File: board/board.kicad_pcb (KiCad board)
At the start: 2 copper layers, 21 x 13 mm, 1 part

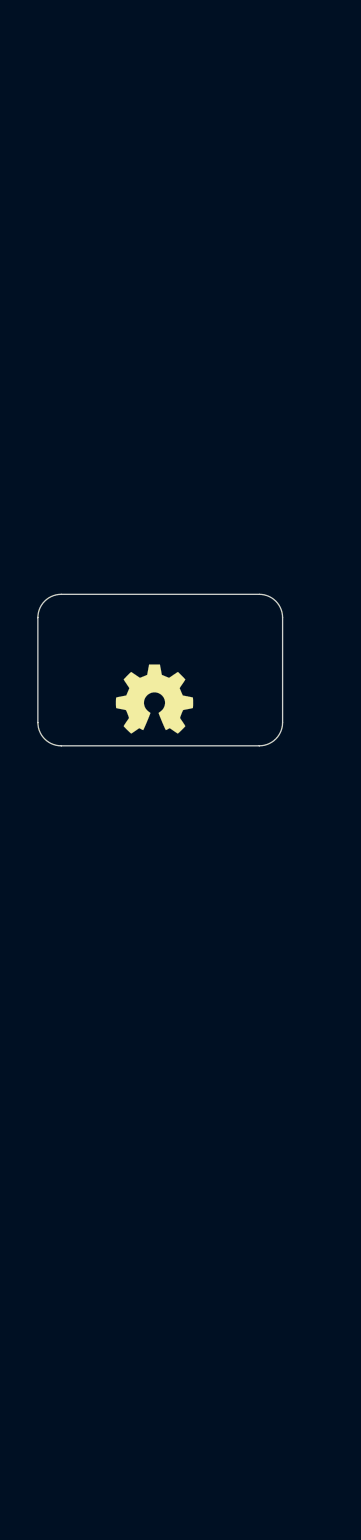
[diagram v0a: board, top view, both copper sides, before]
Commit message: added decoupling components
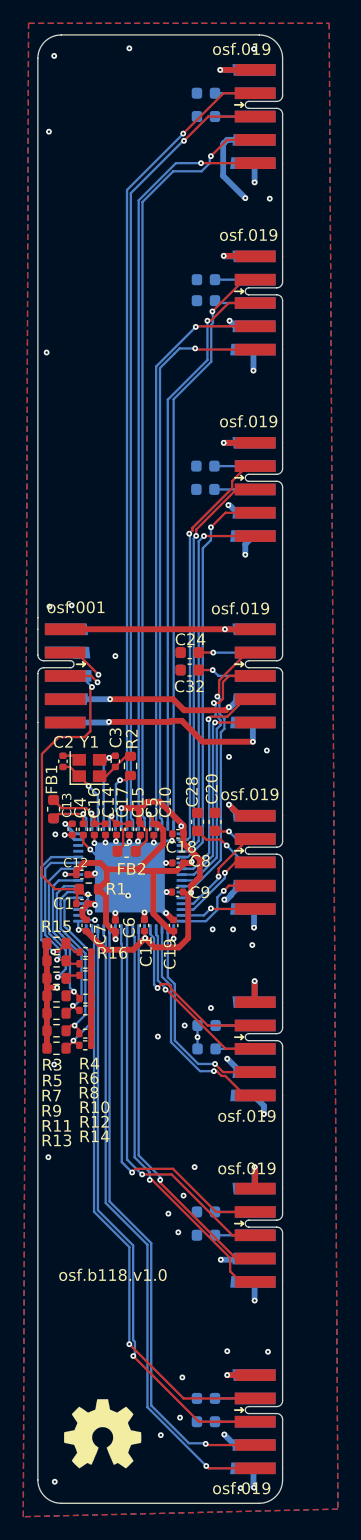
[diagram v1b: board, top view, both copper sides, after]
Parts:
- added C1: 10uF, Capacitor_SMD:C_0402_1005Metric, F.Cu at (143.8, 116.5)
- added C10: 1uF, Capacitor_SMD:C_0402_1005Metric, F.Cu at (149.9, 110.2)
- added C11: 1uF, Capacitor_SMD:C_0402_1005Metric, F.Cu at (149.2, 118.4)
- added C12: 1uF, Capacitor_SMD:C_0402_1005Metric, F.Cu at (143.8, 114.0)
- added C13: 1uF, Capacitor_SMD:C_0402_1005Metric, F.Cu at (142.9, 110.2)
- added C14: 10uF, Capacitor_SMD:C_0402_1005Metric, F.Cu at (145.8, 110.2)
- added C15: 10uF, Capacitor_SMD:C_0402_1005Metric, F.Cu at (147.8, 110.2)
- added C16: 1uF, Capacitor_SMD:C_0402_1005Metric, F.Cu at (144.8, 110.2)
- added C17: 1uF, Capacitor_SMD:C_0402_1005Metric, F.Cu at (146.8, 110.2)
- added C18: 1uF, Capacitor_SMD:C_0402_1005Metric, F.Cu at (152.0, 110.5)
- added C19: 1uF, Capacitor_SMD:C_0402_1005Metric, F.Cu at (151.7, 118.4)
- added C2: 22pF, Capacitor_SMD:C_0402_1005Metric, F.Cu at (142.2, 104.3)
- added C20: 100nF, Capacitor_SMD:C_0603_1608Metric, F.Cu at (155.2, 109.5)
- added C21: 100nF, Capacitor_SMD:C_0603_1608Metric, B.Cu at (154.5, 127.0)
- added C22: 100nF, Capacitor_SMD:C_0603_1608Metric, B.Cu at (154.4, 143.0)
- added C23: 100nF, Capacitor_SMD:C_0603_1608Metric, B.Cu at (154.4, 79.0)
- added C24: 100nF, Capacitor_SMD:C_0603_1608Metric, F.Cu at (153.0, 95.0)
- added C25: 100nF, Capacitor_SMD:C_0603_1608Metric, B.Cu at (154.4, 159.0)
- added C26: 100nF, Capacitor_SMD:C_0603_1608Metric, B.Cu at (154.4, 63.0)
- added C27: 100nF, Capacitor_SMD:C_0603_1608Metric, B.Cu at (154.4, 47.0)
- added C28: 100nF, Capacitor_SMD:C_0603_1608Metric, F.Cu at (153.7, 109.5)
- added C29: 100nF, Capacitor_SMD:C_0603_1608Metric, B.Cu at (154.5, 129.0)
- added C3: 22pF, Capacitor_SMD:C_0402_1005Metric, F.Cu at (146.7, 104.3)
- added C30: 100nF, Capacitor_SMD:C_0603_1608Metric, B.Cu at (154.4, 145.0)
- added C31: 100nF, Capacitor_SMD:C_0603_1608Metric, B.Cu at (154.4, 81.0)
- added C32: 100nF, Capacitor_SMD:C_0603_1608Metric, F.Cu at (153.0, 96.5)
- added C33: 100nF, Capacitor_SMD:C_0603_1608Metric, B.Cu at (154.4, 161.0)
- added C34: 100nF, Capacitor_SMD:C_0603_1608Metric, B.Cu at (154.4, 64.8)
- added C35: 100nF, Capacitor_SMD:C_0603_1608Metric, B.Cu at (154.4, 49.0)
- added C4: 10uF, Capacitor_SMD:C_0402_1005Metric, F.Cu at (143.9, 110.2)
- added C5: 10uF, Capacitor_SMD:C_0402_1005Metric, F.Cu at (148.8, 110.2)
- added C6: 1uF, Capacitor_SMD:C_0402_1005Metric, F.Cu at (146.7, 118.5)
- added C7: 1uF, Capacitor_SMD:C_0402_1005Metric, F.Cu at (144.2, 118.4)
- added C8: 1uF, Capacitor_SMD:C_0402_1005Metric, F.Cu at (152.0, 113.0)
- added C9: 1uF, Capacitor_SMD:C_0402_1005Metric, F.Cu at (152.0, 115.5)
- added FB1: Ferrite_Bead_Small, Inductor_SMD:L_0603_1608Metric, F.Cu at (141.3, 108.4)
- added FB2: Ferrite_Bead_Small, Inductor_SMD:L_0603_1608Metric, F.Cu at (147.6, 112.0)
- added IC1: RTL8305NB-CG, Package_DFN_QFN:QFN-64-1EP_9x9mm_P0.5mm_EP6x6mm, B.Cu at (147.9, 114.3)
- added J1: 001_I2C, on_edge:on_edge_2x05_device, F.Cu at (140.0, 97.0)
- added J2: 019_100BASE-T_with_CT, on_edge:on_edge_2x05_host, F.Cu at (161.0, 113.0)
- added J3: 019_100BASE-T_with_CT, on_edge:on_edge_2x05_host, F.Cu at (161.0, 129.0)
- added J4: 019_100BASE-T_with_CT, on_edge:on_edge_2x05_host, F.Cu at (161.0, 145.0)
- added J5: 019_100BASE-T_with_CT, on_edge:on_edge_2x05_host, F.Cu at (161.0, 161.0)
- added J6: 019_100BASE-T_with_CT, on_edge:on_edge_2x05_host, F.Cu at (161.0, 97.0)
- added J7: 019_100BASE-T_with_CT, on_edge:on_edge_2x05_host, F.Cu at (161.0, 65.0)
- added J8: 019_100BASE-T_with_CT, on_edge:on_edge_2x05_host, F.Cu at (161.0, 81.0)
- added J9: 019_100BASE-T_with_CT, on_edge:on_edge_2x05_host, F.Cu at (161.0, 49.0)
- added R1: 10k, Resistor_SMD:R_0603_1608Metric, F.Cu at (144.4, 115.3)
- added R10: d.n.p, Resistor_SMD:R_0402_1005Metric, F.Cu at (144.1, 125.7)
- added R11: 1k, Resistor_SMD:R_0603_1608Metric, F.Cu at (141.6, 127.5)
- added R12: d.n.p, Resistor_SMD:R_0402_1005Metric, F.Cu at (144.1, 127.7)
- added R13: 1k, Resistor_SMD:R_0603_1608Metric, F.Cu at (141.6, 128.9)
- added R14: d.n.p, Resistor_SMD:R_0402_1005Metric, F.Cu at (144.1, 128.7)
- added R15: 1k, Resistor_SMD:R_0603_1608Metric, F.Cu at (141.6, 120.0)
- added R16: d.n.p, Resistor_SMD:R_0402_1005Metric, F.Cu at (144.1, 120.7)
- added R2: 2.49k, Resistor_SMD:R_0603_1608Metric, F.Cu at (147.9, 104.7)
- added R3: 1k, Resistor_SMD:R_0603_1608Metric, F.Cu at (141.6, 121.5)
- added R4: d.n.p, Resistor_SMD:R_0402_1005Metric, F.Cu at (144.1, 121.7)
- added R5: 1k, Resistor_SMD:R_0603_1608Metric, F.Cu at (141.6, 123.0)
- added R6: d.n.p, Resistor_SMD:R_0402_1005Metric, F.Cu at (144.1, 122.7)
- added R7: 1k, Resistor_SMD:R_0603_1608Metric, F.Cu at (141.6, 124.5)
- added R8: d.n.p, Resistor_SMD:R_0402_1005Metric, F.Cu at (144.1, 124.7)
- added R9: 1k, Resistor_SMD:R_0603_1608Metric, F.Cu at (141.6, 126.0)
- added Y1: 25Mhz, Crystal:Crystal_SMD_2520-4Pin_2.5x2.0mm, F.Cu at (144.4, 104.9)
- moved LOGO1 63.2 mm to (145.6, 162.1)
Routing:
- net +3.3V: track 0.00 -> 216.0 mm, vias 0 -> 16
- net +5V: track 0.00 -> 152.6 mm, vias 0 -> 9
- net GND: track 0.00 -> 138.4 mm, vias 0 -> 57
- net /switch/RXP0: track 0.00 -> 69.0 mm, vias 0 -> 1
- net /switch/RXM0: track 0.00 -> 67.8 mm, vias 0 -> 1
- net /switch/TXP0: track 0.00 -> 65.8 mm, vias 0 -> 1
- net /switch/TXM0: track 0.00 -> 65.0 mm, vias 0 -> 1
- net /switch/TXM7: track 0.00 -> 54.0 mm, vias 0 -> 1
- net /switch/TXP7: track 0.00 -> 52.7 mm, vias 0 -> 1
- net /switch/RXM7: track 0.00 -> 50.8 mm, vias 0 -> 1
- net /switch/RXP1: track 0.00 -> 50.4 mm, vias 0 -> 1
- net /switch/1.0V: track 0.00 -> 50.2 mm, vias 0 -> 6
- net /switch/RXP7: track 0.00 -> 49.7 mm, vias 0 -> 1
- net /switch/RXM1: track 0.00 -> 49.5 mm, vias 0 -> 1
- net /switch/TXP1: track 0.00 -> 49.3 mm, vias 0 -> 1
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- added copper zone on In1.Cu, net +3.3V
- added copper zone on B.Cu, net GND
- added copper zone on F.Cu, net GND
- added copper zone on In2.Cu, net GND
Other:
- board size 21 x 13 mm -> 21 x 126 mm
- copper layers 2 -> 4
- board text added: "osf.001"
- board text added: "osf.019"
- board text added: "osf.b118.v1.0"
